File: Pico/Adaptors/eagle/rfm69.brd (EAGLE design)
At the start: 25.7 x 18.4 mm, 3 parts

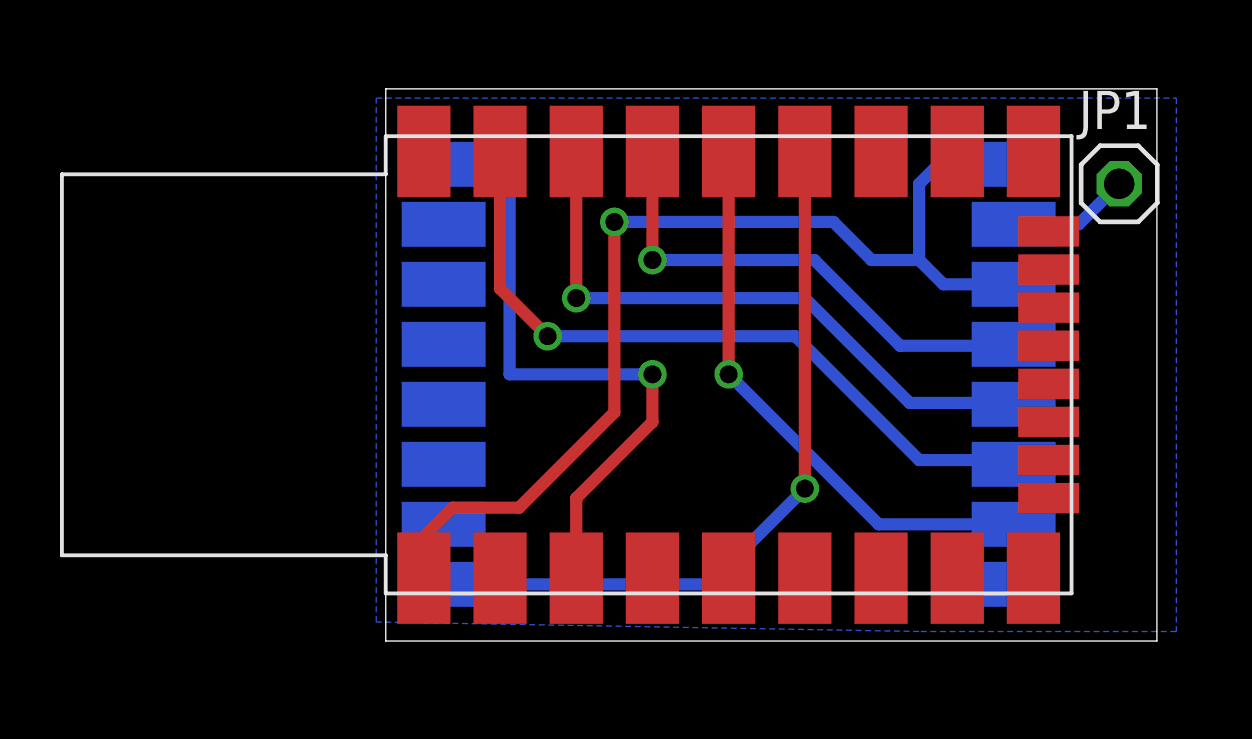
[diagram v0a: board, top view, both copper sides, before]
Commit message: added robot shield, and tweaked RFM69 shim (getting protos made)
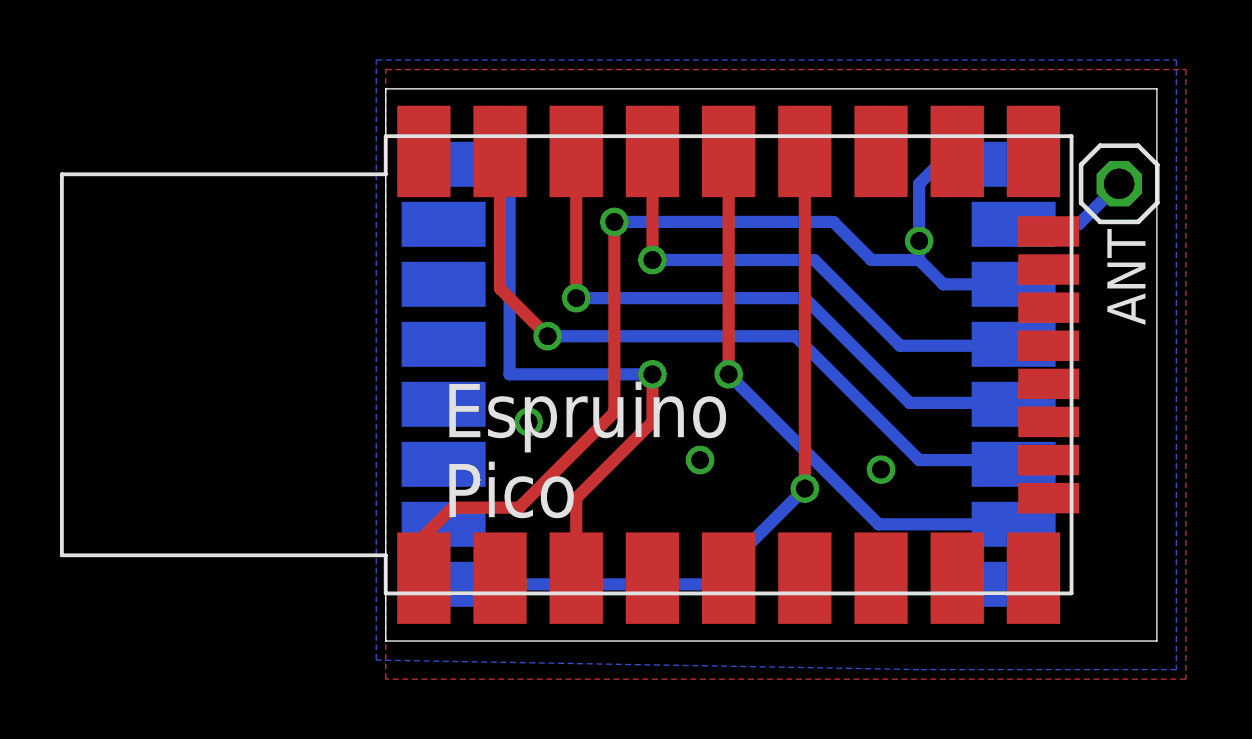
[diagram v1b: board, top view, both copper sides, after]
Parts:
- renumbered JP1 to ANT
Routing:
- net GND: vias 1 -> 5
- added copper zone on layer 1, net GND
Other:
- board text added: "Espruino Pico"
- board text added: "RFM69HW"
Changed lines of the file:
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@@
 <wire x1="25.705" y1="18.405" x2="0" y2="18.405" width="0" layer="20"/>
 <wire x1="0" y1="18.405" x2="0" y2="0" width="0" layer="20"/>
+<text x="1.905" y="4.1275" size="1.778" layer="25">Espruino
+Pico</text>
+<text x="19.05" y="10.16" size="1.778" layer="26" rot="MR0">RFM69HW</text>
 </plain>
 <attributes>
@@
 </class>
 </classes>
-<designrules name="oshpark">
+<designrules name="oshpark *">
 <description language="de">&lt;b&gt;EAGLE Design Rules&lt;/b&gt;
 &lt;p&gt;
@@
 <param name="mlMinCreamFrame" value="0mil"/>
 <param name="mlMaxCreamFrame" value="0mil"/>
-<param name="mlViaStopLimit" value="15mil"/>
+<param name="mlViaStopLimit" value="30mil"/>
 <param name="srRoundness" value="0"/>
 <param name="srMinRoundness" value="0mil"/>
@@
 <elements>
 <element name="U$1" library="espruino_pico" package="ESPRUINO_PICO_SMDONLY" value="ESPRUINO_PICO_SMDONLY" x="15.24" y="9.2075"/>
-<element name="JP1" library="pinhead" package="1X01" value="" x="24.4475" y="15.24"/>
+<element name="ANT" library="pinhead" package="1X01" value="" x="24.4475" y="15.24" smashed="yes">
+<attribute name="NAME" x="24.0538" y="13.7287" size="1.27" layer="25" ratio="10" rot="R270"/>
+<attribute name="VALUE" x="23.1775" y="12.065" size="1.27" layer="27"/>
+</element>
 <element name="U$3" library="RFM69" package="RFM69" value="RFM69" x="11.43" y="8.89" rot="MR180"/>
 </elements>
@@
 <contactref element="U$1" pad="GND"/>
 <polygon width="0.4064" layer="16">
-<vertex x="-0.3175" y="18.0975"/>
-<vertex x="26.3525" y="18.0975"/>
-<vertex x="26.3525" y="0.3175"/>
-<vertex x="17.78" y="0.3175"/>
-<vertex x="-0.3175" y="0.635"/>
+<vertex x="-0.3175" y="19.3675"/>
+<vertex x="26.3525" y="19.3675"/>
+<vertex x="26.3525" y="-0.9525"/>
+<vertex x="17.78" y="-0.9525"/>
+<vertex x="-0.3175" y="-0.635"/>
 </polygon>
 <contactref element="U$3" pad="P$11"/>
@@
 <wire x1="2.2225" y1="4.445" x2="1.27" y2="3.4925" width="0.4064" layer="1"/>
 <wire x1="1.27" y1="3.4925" x2="1.27" y2="2.0955" width="0.4064" layer="1"/>
+<via x="17.78" y="13.335" extent="1-16" drill="0.6"/>
+<via x="16.51" y="5.715" extent="1-16" drill="0.6"/>
+<via x="10.4775" y="6.0325" extent="1-16" drill="0.6"/>
+<via x="4.7625" y="7.3025" extent="1-16" drill="0.6"/>
+<wire x1="17.78" y1="13.335" x2="16.51" y2="5.715" width="0" layer="19" extent="1-1"/>
+<wire x1="4.7625" y1="7.3025" x2="7.62" y2="7.62" width="0" layer="19" extent="1-1"/>
+<polygon width="0.4064" layer="1">
+<vertex x="0" y="19.05"/>
+<vertex x="26.67" y="19.05"/>
+<vertex x="26.67" y="-1.27"/>
+<vertex x="0" y="-1.27"/>
+</polygon>
 </signal>
 <signal name="3.3V">
@@
 </signal>
 <signal name="N$1">
-<contactref element="JP1" pad="1"/>
+<contactref element="ANT" pad="1"/>
 <contactref element="U$3" pad="P$10"/>
 <wire x1="20.93" y1="13.89" x2="23.0975" y2="13.89" width="0.4064" layer="16"/>
@@
 </board>
 </drawing>
+<compatibility>
+<note version="6.3" minversion="6.2.2" severity="warning">
+Since Version 6.2.2 text objects can contain more than one line,
+which will not be processed correctly with this version.
+</note>
+</compatibility>
 </eagle>

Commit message: add irq line
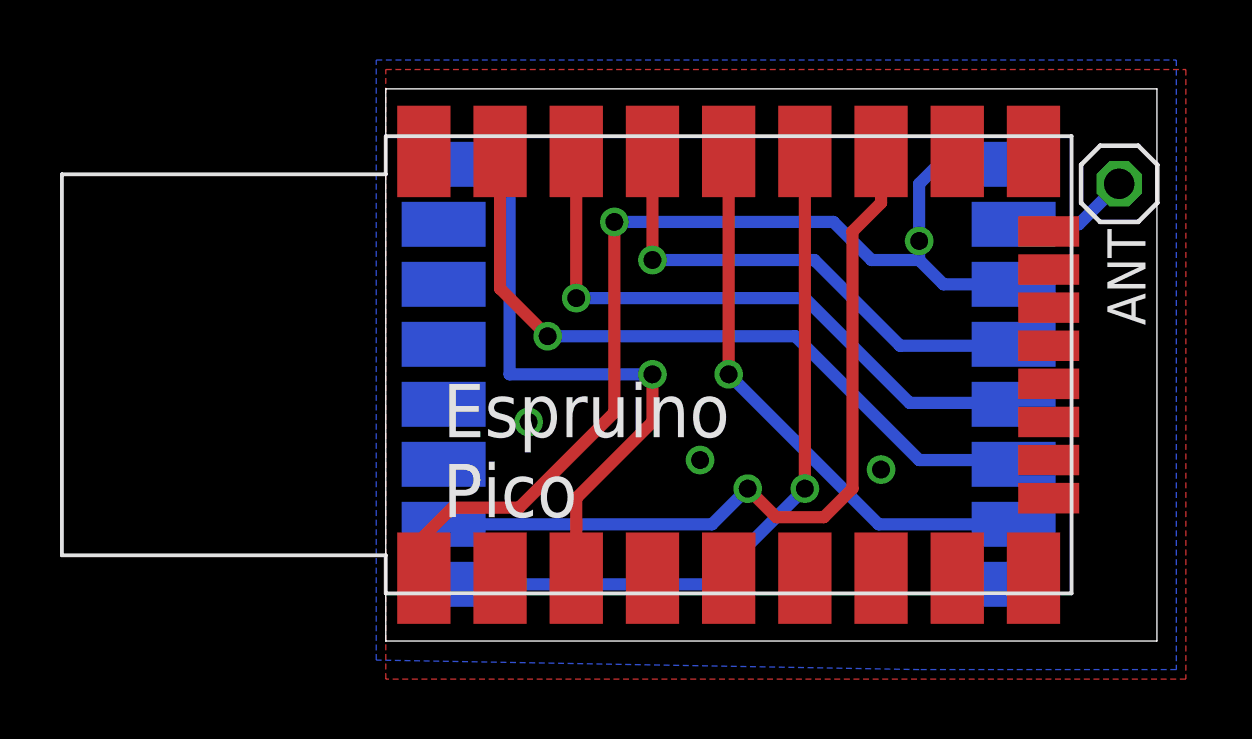
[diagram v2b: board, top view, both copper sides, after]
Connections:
- new net IRQ: U$1.A7, U$3.P$2
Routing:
- net IRQ: track 0.00 -> 26.5 mm, vias 0 -> 1
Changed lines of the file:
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@@
 <wire x1="13.97" y1="5.08" x2="13.97" y2="16.3195" width="0.4064" layer="1"/>
+</signal>
+<signal name="IRQ">
+<contactref element="U$3" pad="P$2"/>
+<contactref element="U$1" pad="A7"/>
+<wire x1="1.93" y1="3.89" x2="10.875" y2="3.89" width="0.4064" layer="16"/>
+<wire x1="10.875" y1="3.89" x2="12.065" y2="5.08" width="0.4064" layer="16"/>
+<via x="12.065" y="5.08" extent="1-16" drill="0.6"/>
+<wire x1="12.065" y1="5.08" x2="13.0175" y2="4.1275" width="0.4064" layer="1"/>
+<wire x1="13.0175" y1="4.1275" x2="14.605" y2="4.1275" width="0.4064" layer="1"/>
+<wire x1="14.605" y1="4.1275" x2="15.5575" y2="5.08" width="0.4064" layer="1"/>
+<wire x1="15.5575" y1="5.08" x2="15.5575" y2="13.6525" width="0.4064" layer="1"/>
+<wire x1="15.5575" y1="13.6525" x2="16.51" y2="14.605" width="0.4064" layer="1"/>
+<wire x1="16.51" y1="14.605" x2="16.51" y2="16.3195" width="0.4064" layer="1"/>
 </signal>
 </signals>
